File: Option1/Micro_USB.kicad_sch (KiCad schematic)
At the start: 15 parts, among them J1401 10118194-0001LF, J1402 Conn_01x06_Pin, Q1401 BC817-40, Q1402 BC817-40, U1401 CH340X

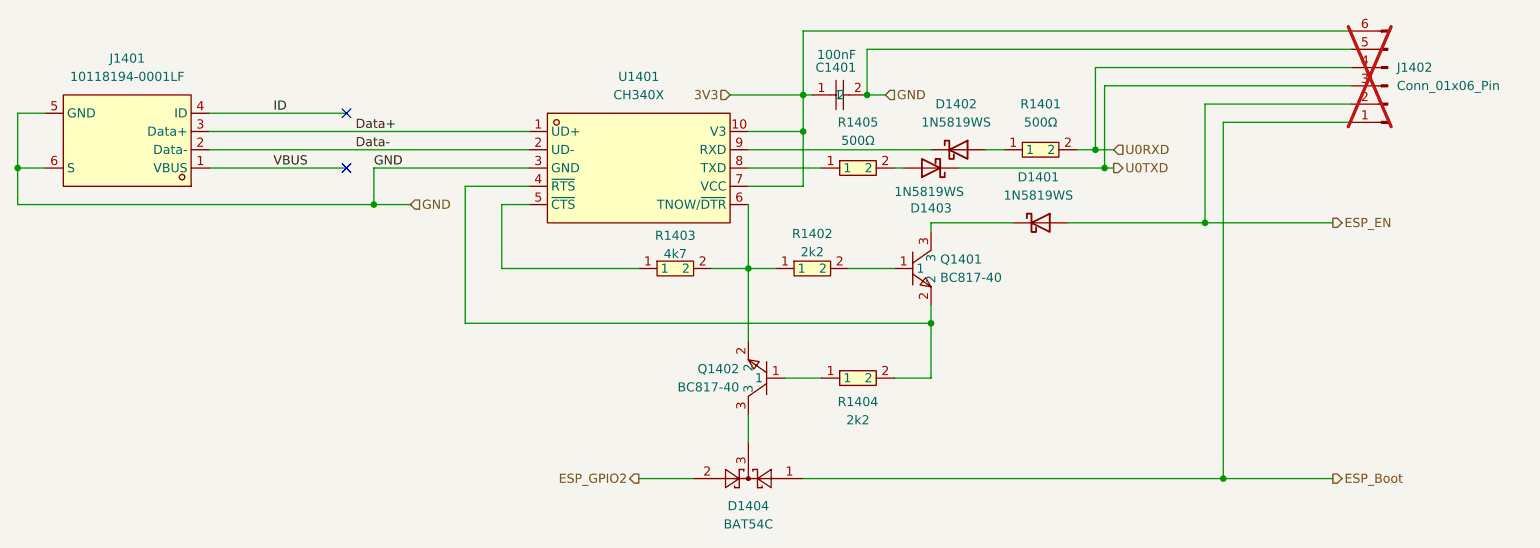
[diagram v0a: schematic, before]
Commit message: Kapitel über Schaltplan fortgesetzt, Fehler in Schaltplan korrigiert, DCDC getauscht, USB Schaltung angepasst, 3.3V Schaltung angepasst
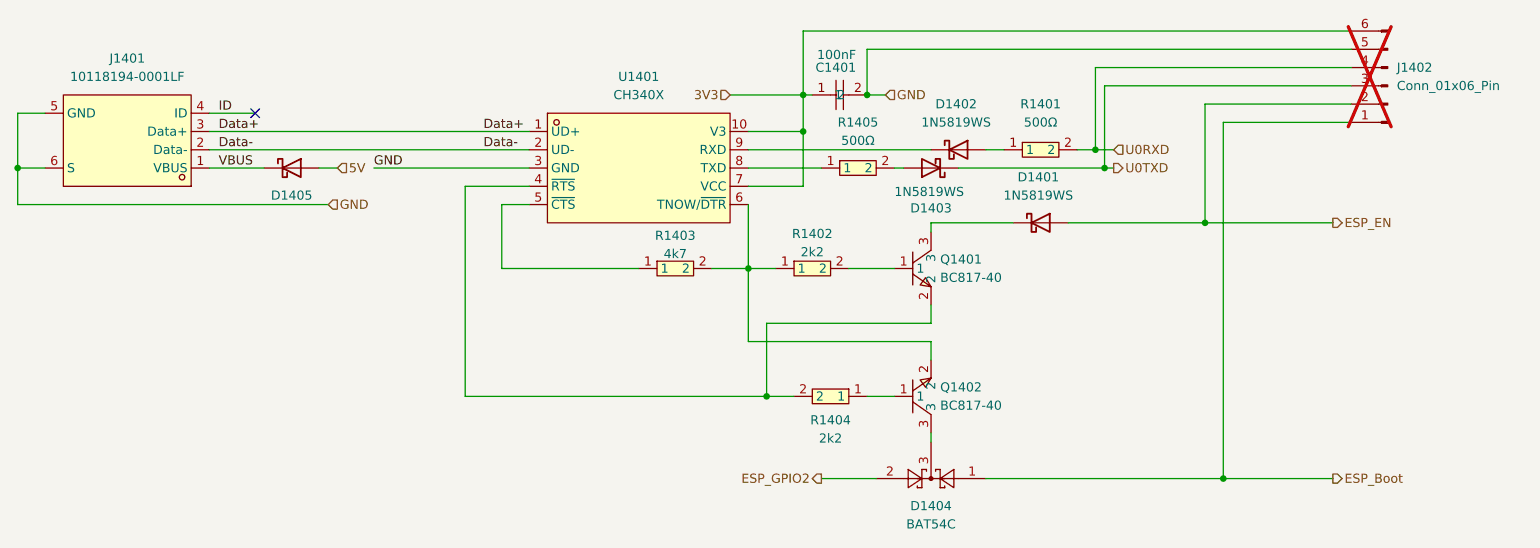
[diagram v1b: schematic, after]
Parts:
- added D1405: 1N5819WS, Diode_SMD:D_SOD-323, symbol Diode:1N5819WS
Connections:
- net VBUS: now also D1405.1 (K)
- new net 5V: D1405.2 (A)
- no-connect marks 2 -> 1
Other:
- moved on the sheet: D1404, Q1402, R1404

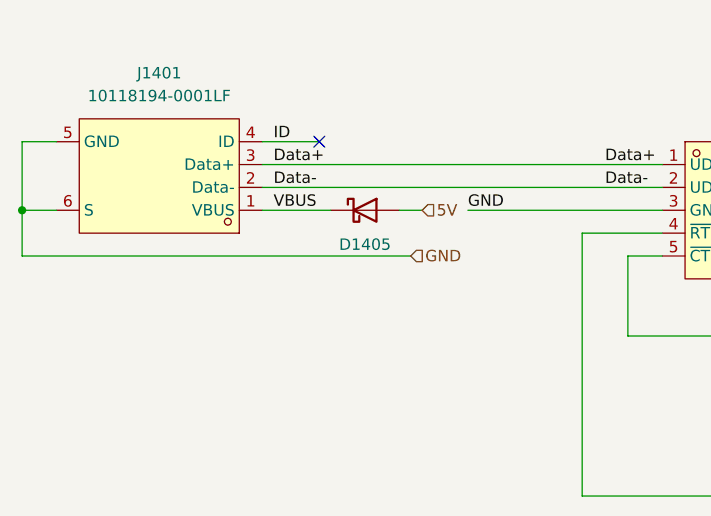
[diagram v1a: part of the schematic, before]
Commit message: Platine korrigeiert, 5V DCDC getauscht, 3.3V Display Versorgung entfernt. Bauteile neu angeordnet, USB 5V auf 5V Supply geführt
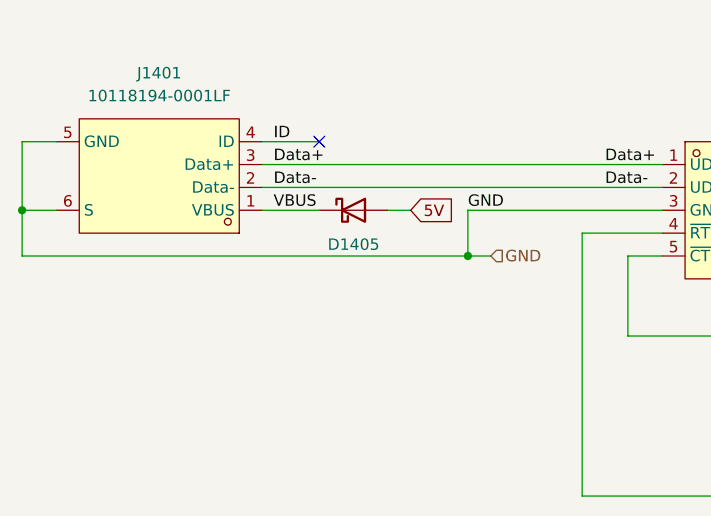
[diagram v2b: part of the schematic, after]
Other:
- moved on the sheet: D1405
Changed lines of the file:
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@@
+	)
+	(junction
+		(at 68.58 60.96)
+		(diameter 0)
+		(color 0 0 0 0)
 	)
 	(junction
@@
 	(wire
 		(pts
-			(xy 45.72 55.88) (xy 53.34 55.88)
+			(xy 45.72 55.88) (xy 52.07 55.88)
 		)
 		(stroke
@@
 	(wire
 		(pts
+			(xy 68.58 60.96) (xy 71.12 60.96)
+		)
+		(stroke
+			(width 0)
+			(type default)
+		)
+	)
+	(wire
+		(pts
 			(xy 129.54 45.72) (xy 128.27 45.72)
 		)
@@
 	(wire
 		(pts
+			(xy 68.58 55.88) (xy 68.58 60.96)
+		)
+		(stroke
+			(width 0)
+			(type default)
+		)
+	)
+	(wire
+		(pts
 			(xy 168.91 41.91) (xy 168.91 53.34)
 		)
@@
 	(wire
 		(pts
-			(xy 19.05 60.96) (xy 62.23 60.96)
+			(xy 19.05 60.96) (xy 68.58 60.96)
 		)
 		(stroke
@@
 	(wire
 		(pts
-			(xy 60.96 55.88) (xy 63.5 55.88)
+			(xy 59.69 55.88) (xy 62.23 55.88)
 		)
 		(stroke
@@
 			)
 			(justify left bottom)
+		)
+	)
+	(global_label "5V"
+		(shape input)
+		(at 62.23 55.88 0)
+		(fields_autoplaced yes)
+		(effects
+			(font
+				(size 1.27 1.27)
+			)
+			(justify left)
+		)
+		(property "Intersheetrefs" "${INTERSHEET_REFS}"
+			(at 67.5133 55.88 0)
+			(effects
+				(font
+					(size 1.27 1.27)
+				)
+				(justify left)
+				(hide yes)
+			)
 		)
 	)
@@
 		)
 	)
-	(hierarchical_label "5V"
-		(shape input)
-		(at 63.5 55.88 0)
-		(effects
-			(font
-				(size 1.27 1.27)
-			)
-			(justify left)
-		)
-	)
 	(hierarchical_label "3V3"
 		(shape input)
@@
 	(hierarchical_label "GND"
 		(shape input)
-		(at 62.23 60.96 0)
+		(at 71.12 60.96 0)
 		(effects
 			(font
@@
 	(symbol
 		(lib_id "Diode:1N5819WS")
-		(at 57.15 55.88 0)
+		(at 55.88 55.88 0)
 		(unit 1)
 		(exclude_from_sim no)
@@
 		(dnp no)
 		(property "Reference" "D1405"
-			(at 57.15 59.69 0)
+			(at 55.88 59.69 0)
 			(effects
 				(font
@@
 		)
 		(property "Value" "1N5819WS"
-			(at 56.8325 52.07 0)
+			(at 55.5625 52.07 0)
 			(effects
 				(font
@@
 		)
 		(property "Footprint" "Diode_SMD:D_SOD-323"
-			(at 57.15 60.325 0)
+			(at 55.88 60.325 0)
 			(effects
 				(font
@@
 		)
 		(property "Datasheet" "https://datasheet.lcsc.com/lcsc/2204281430_Guangdong-Hottech-1N5819WS_C191023.pdf"
-			(at 57.15 55.88 0)
+			(at 55.88 55.88 0)
 			(effects
 				(font
@@
 		)
 		(property "Description" "40V 600mV@1A 1A SOD-323 Schottky Barrier Diodes, SOD-323"
-			(at 57.15 55.88 0)
-			(effects
-				(font
+			(at 55.88 55.88 0)
+			(effects
+				(font

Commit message: USB Beschaltung teilweise korrigiert, Fehlerbehebung steht aus
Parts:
- removed D1405: 1N5819WS, Diode_SMD:D_SOD-323, symbol Diode:1N5819WS
- added C1401: 22uF / 6.3V, easyeda2kicad:C0603, symbol easyeda2kicad:CL10A226MQ8NRNC
- added D1405: SS14, easyeda2kicad:SMA_L4.2-W2.6-LS5.3-RD, symbol easyeda2kicad:SS14
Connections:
- net 5V: now also D1405.1 (K)
- net GND: now also C1401.1
- net U0TXD: now also D1402.2 (A); no longer D1403.1 (K)
- net VBUS: now also C1401.2, D1405.2 (A)
- net at R1401.1: now also D1403.1 (K); no longer D1402.2 (A)
- net at U1401.9 (RXD): now also D1403.2 (A); no longer D1402.1 (K)
- net at R1405.2: now also D1402.1 (K); no longer D1403.2 (A)
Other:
- moved on the sheet: D1402, D1403

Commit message: Fertigfe Abschlusspräsentation
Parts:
- removed J1402: Conn_01x06_Pin, Connector_PinSocket_2.54mm:PinSocket_1x06_P2.54mm_Vertical, symbol Connector:Conn_01x06_Pin
